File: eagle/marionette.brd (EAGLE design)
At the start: 139.7 x 76.2 mm, 228 parts, among them J17 MA02-1, J18 MA02-1, J19 MA02-1, J2 SWD, J20 MA02-1, J22 ZX62D-B-5P8, J6 MA03-2W, J8 MA04-2W, Q1 BSS84, U1 STM32F407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

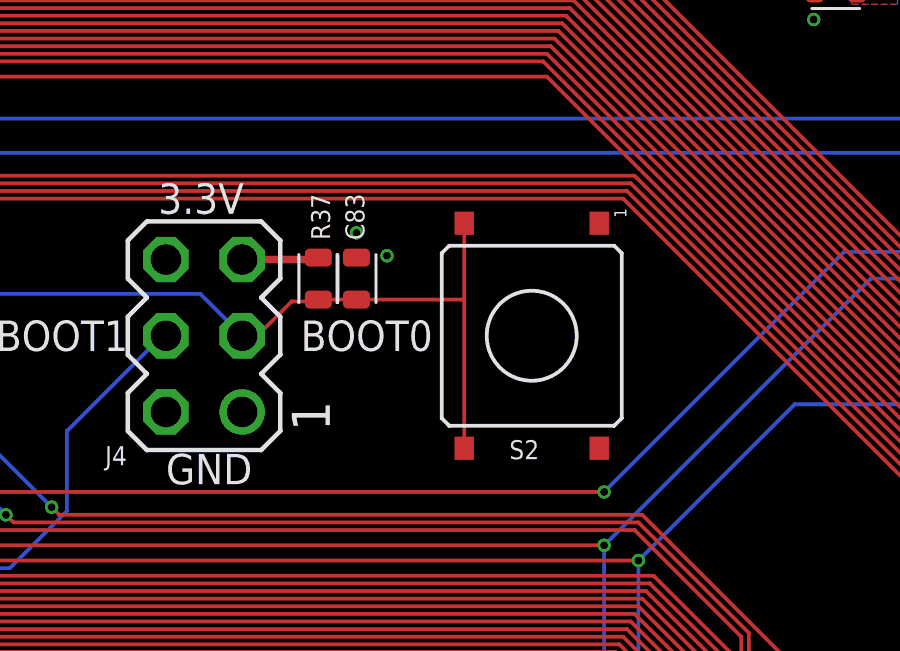
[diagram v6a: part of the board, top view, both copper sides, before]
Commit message: fixed boot0 switch for DFU
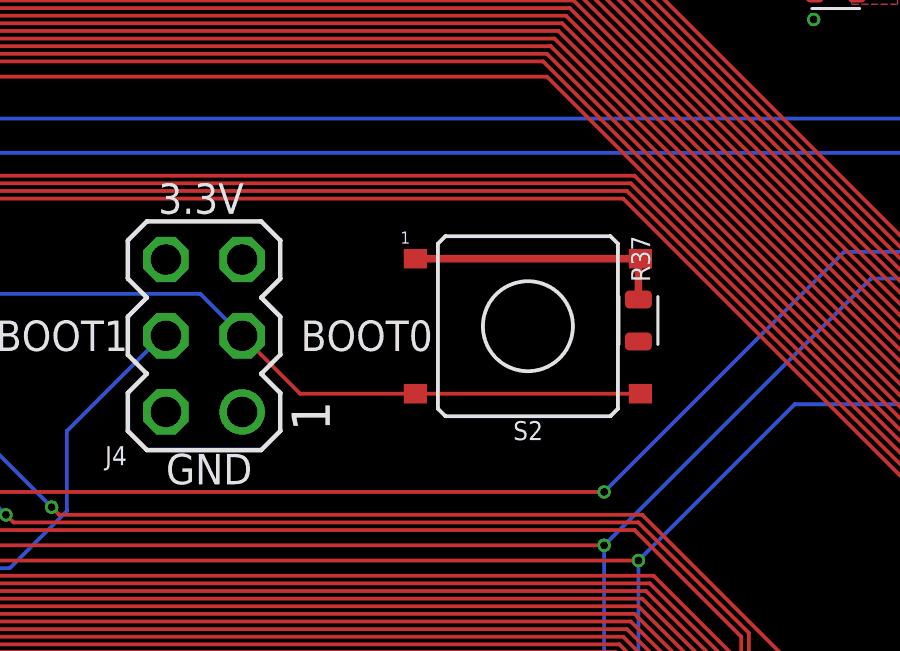
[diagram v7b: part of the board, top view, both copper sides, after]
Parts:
- removed C83: 100nF, 10V, rcl_custom:.0603-C
- moved R37 10.8 mm to (96.0, 53.0)
- moved S2 0.34 mm to (92.3, 52.8), turned to 0 degrees
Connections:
- new net N$37: R37.2, S2.1, S2.2
- net 3.3VDD: no longer R37.2
- net BOOT0: no longer C83.1, R37.1
- net GND: now also R37.1; no longer C83.2, S2.1, S2.2
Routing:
- net N$37: track 0.00 -> 8.89 mm
- net 3.3VDD: track 21.9 -> 19.3 mm
- net BOOT0: track 71.9 -> 70.6 mm
- net GND: vias 416 -> 414
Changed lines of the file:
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@@
 <setting verticaltext="up"/>
 </settings>
-<grid distance="0.005" unitdist="inch" unit="inch" style="lines" multiple="4" display="yes" altdistance="0.025" altunitdist="inch" altunit="inch"/>
+<grid distance="0.0025" unitdist="inch" unit="inch" style="lines" multiple="4" display="yes" altdistance="0.025" altunitdist="inch" altunit="inch"/>
 <layers>
 <layer number="1" name="Top" color="4" fill="1" visible="yes" active="yes"/>
@@
 <attribute name="NAME" x="18.997" y="8.648" size="0.7" layer="25" font="vector" rot="R90"/>
 </element>
-<element name="S2" library="PTS645" package="SMT" value="PTS645" x="92.456" y="52.451" smashed="yes" rot="R270">
-<attribute name="NAME" x="91.71" y="48.335" size="0.635" layer="25" font="vector" ratio="20"/>
-</element>
-<element name="C83" library="rcl_custom" package=".0603-C" value="100nF, 10V" x="86.614" y="54.356" smashed="yes" rot="R90">
-<attribute name="NAME" x="86.88" y="55.642" size="0.635" layer="25" font="vector" ratio="15" rot="R90"/>
-<attribute name="NAME" x="86.614" y="54.356" size="0.3" layer="33" ratio="15" rot="R90" align="center"/>
+<element name="S2" library="PTS645" package="SMT" value="PTS645" x="92.329" y="52.7685" smashed="yes">
+<attribute name="NAME" x="91.837" y="48.97" size="0.635" layer="25" font="vector" ratio="20"/>
 </element>
 <element name="SCL" library="Tova" package="10MIL-TEST-POINT" value="TEST-POINT10MIL-TEST-POINT" x="18.619" y="12.635" smashed="yes">
@@
 <attribute name="NAME" x="36.576" y="30.861" size="0.3" layer="33" ratio="15" align="center"/>
 </element>
-<element name="R37" library="rcl_custom" package=".0603-C" value="10k" x="85.344" y="54.356" smashed="yes" rot="R90">
-<attribute name="NAME" x="85.737" y="55.642" size="0.635" layer="25" font="vector" ratio="15" rot="R90"/>
-<attribute name="VALUE" x="86.894" y="53.356" size="0.8" layer="27" font="vector" ratio="15" rot="R90"/>
-<attribute name="NAME" x="85.344" y="54.356" size="0.3" layer="33" ratio="15" rot="R90" align="center"/>
+<element name="R37" library="rcl_custom" package=".0603-C" value="10k" x="96.012" y="52.959" smashed="yes" rot="R90">
+<attribute name="NAME" x="96.405" y="54.245" size="0.635" layer="25" font="vector" ratio="15" rot="R90"/>
+<attribute name="VALUE" x="97.562" y="51.959" size="0.8" layer="27" font="vector" ratio="15" rot="R90"/>
+<attribute name="NAME" x="96.012" y="52.959" size="0.3" layer="33" ratio="15" rot="R90" align="center"/>
 </element>
 <element name="U14" library="USB3320" package="QFN32-5X5" value="USB3320" x="23.553984375" y="57.8530125" rot="R135">
@@
 <via x="29.591" y="32.766" extent="1-16" drill="0.254"/>
 <via x="33.909" y="40.894" extent="1-16" drill="0.254"/>
-<contactref element="S2" pad="2"/>
-<contactref element="S2" pad="1"/>
-<contactref element="C83" pad="2"/>
 <via x="62.23" y="4.445" extent="1-16" drill="0.254"/>
 <via x="62.23" y="6.985" extent="1-16" drill="0.254"/>
@@
 <via x="55.88" y="65.3542" extent="1-16" drill="0.254"/>
 <via x="53.594" y="67.6402" extent="1-16" drill="0.254"/>
-<via x="86.614" y="55.88" extent="1-16" drill="0.254"/>
-<via x="87.63" y="55.118" extent="1-16" drill="0.254"/>
 <contactref element="U14" pad="PAD"/>
 <contactref element="R1" pad="2"/>
@@
 <via x="64.516" y="54.356" extent="1-16" drill="0.254"/>
 <contactref element="R63" pad="2"/>
+<contactref element="R37" pad="1"/>
 <wire x1="22.352" y1="57.912" x2="23.553984375" y2="57.8530125" width="0" layer="19" extent="1-1"/>
 </signal>
@@
 <vertex x="56.388" y="71.882"/>
 </polygon>
-<contactref element="R37" pad="2"/>
-<wire x1="82.804" y1="54.991" x2="85.344" y2="54.991" width="0.254" layer="1"/>
-<wire x1="85.344" y1="54.991" x2="85.344" y2="55.056" width="0.254" layer="1"/>
 <via x="104.14" y="64.516" extent="1-16" drill="0.254"/>
 <via x="104.14" y="64.008" extent="1-16" drill="0.254"/>
@@
 <contactref element="S2" pad="4"/>
 <contactref element="S2" pad="3"/>
-<contactref element="C83" pad="1"/>
-<wire x1="90.206" y1="56.261" x2="90.206" y2="56.201" width="0.4064" layer="1"/>
-<contactref element="R37" pad="1"/>
-<wire x1="82.804" y1="52.451" x2="83.312" y2="52.451" width="0.127" layer="1"/>
-<wire x1="83.312" y1="52.451" x2="84.455" y2="53.594" width="0.127" layer="1"/>
-<wire x1="84.455" y1="53.594" x2="85.282" y2="53.594" width="0.127" layer="1"/>
-<wire x1="85.282" y1="53.594" x2="85.344" y2="53.656" width="0.254" layer="1"/>
-<wire x1="85.344" y1="53.656" x2="86.614" y2="53.656" width="0.127" layer="1"/>
-<wire x1="90.206" y1="56.201" x2="90.206" y2="53.656" width="0.127" layer="1"/>
-<wire x1="90.206" y1="53.656" x2="86.614" y2="53.656" width="0.127" layer="1"/>
-<wire x1="90.206" y1="53.656" x2="90.206" y2="48.701" width="0.127" layer="1"/>
 <wire x1="61.468" y1="59.69" x2="62.865" y2="59.69" width="0.127" layer="16"/>
 <wire x1="62.865" y1="59.69" x2="68.707" y2="53.848" width="0.127" layer="16"/>
 <wire x1="68.707" y1="53.848" x2="81.407" y2="53.848" width="0.127" layer="16"/>
 <wire x1="81.407" y1="53.848" x2="82.804" y2="52.451" width="0.127" layer="16"/>
+<wire x1="88.579" y1="50.5185" x2="96.079" y2="50.5185" width="0.127" layer="1"/>
+<wire x1="88.579" y1="50.5185" x2="84.7365" y2="50.5185" width="0.127" layer="1"/>
+<wire x1="84.7365" y1="50.5185" x2="82.804" y2="52.451" width="0.127" layer="1"/>
 </signal>
 <signal name="N$14">
@@
 <wire x1="20.44820625" y1="56.515" x2="20.97304375" y2="57.0398375" width="0.127" layer="1"/>
 </signal>
+<signal name="N$37">
+<contactref element="S2" pad="2"/>
+<contactref element="S2" pad="1"/>
+<contactref element="R37" pad="2"/>
+<wire x1="88.579" y1="55.0185" x2="96.079" y2="55.0185" width="0.254" layer="1"/>
+<wire x1="96.012" y1="53.659" x2="96.012" y2="54.9515" width="0.254" layer="1"/>
+<wire x1="96.012" y1="54.9515" x2="96.079" y2="55.0185" width="0.254" layer="1"/>
+</signal>
 </signals>

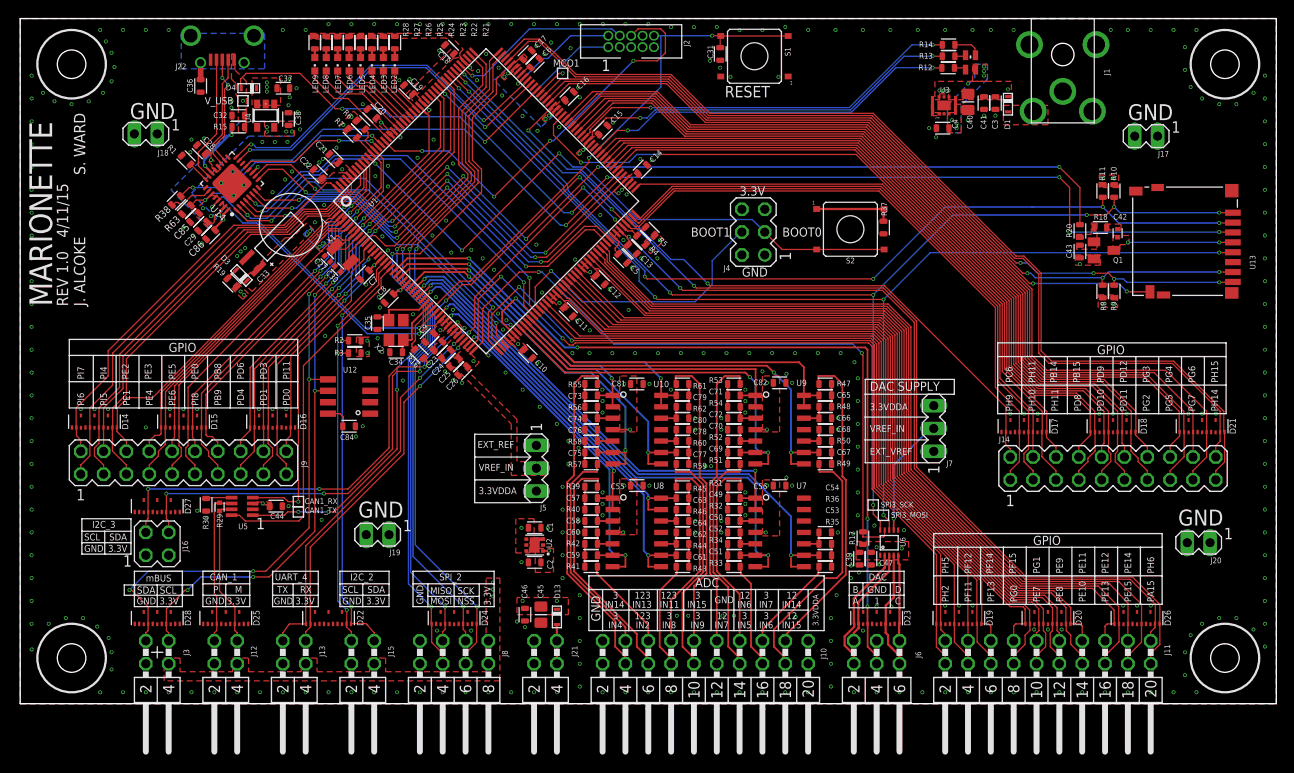
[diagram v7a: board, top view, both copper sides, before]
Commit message: Fixed text size and ratio for tsilk
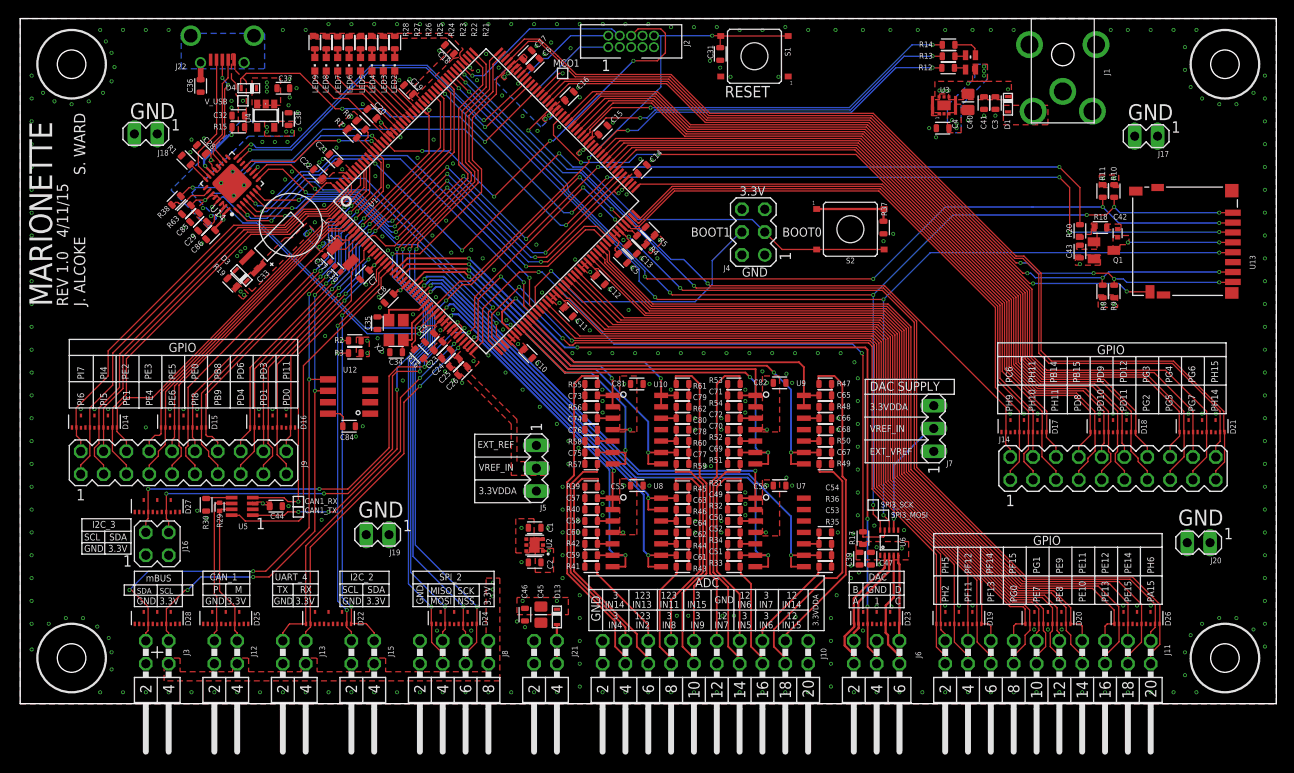
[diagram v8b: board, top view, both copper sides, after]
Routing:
- net GND: vias 414 -> 416
